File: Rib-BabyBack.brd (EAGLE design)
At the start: 67.3 x 74.9 mm, 27 parts, among them IC1 REG1117, SW1 DPDT

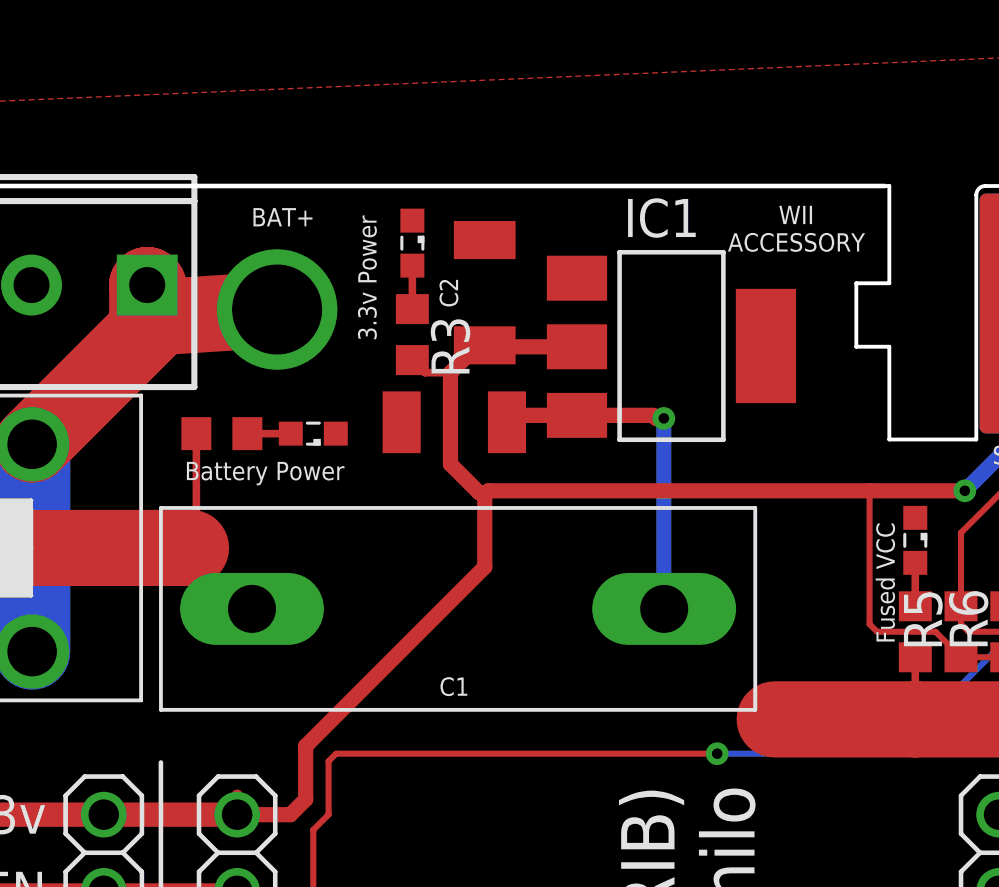
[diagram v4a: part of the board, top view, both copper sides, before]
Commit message: Issue #21 Added a pad for a PTC resetabble fuse for the 3.3v rail
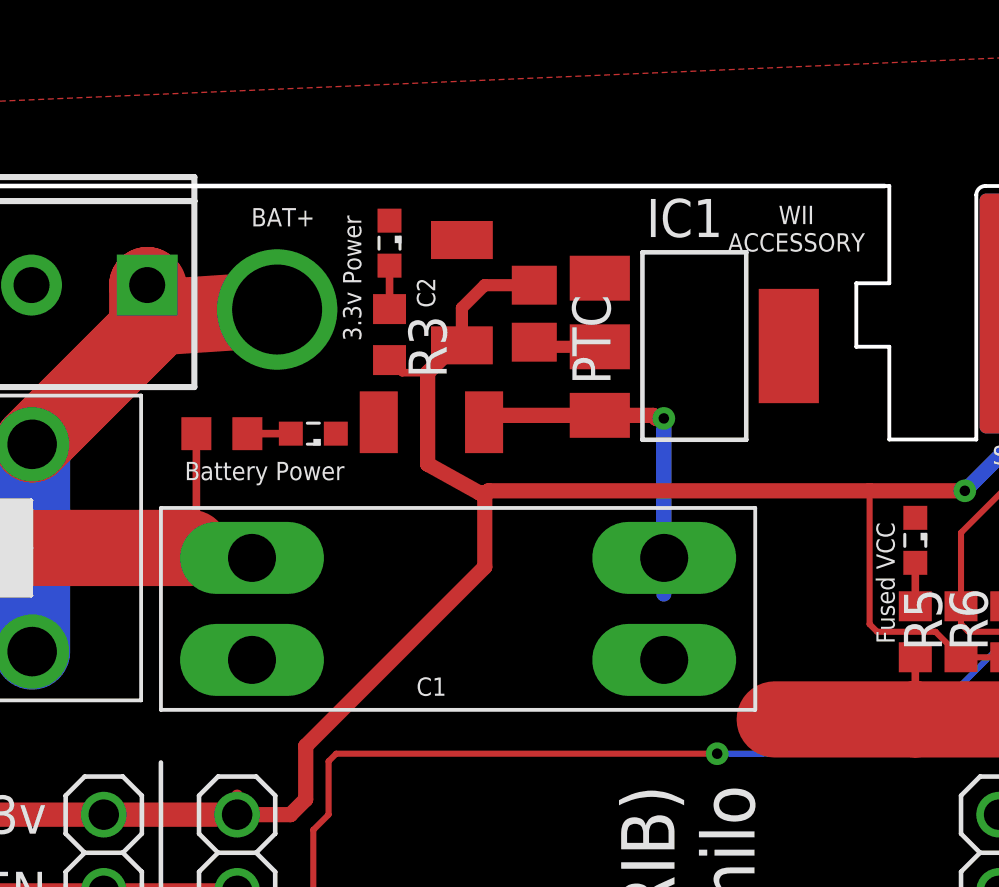
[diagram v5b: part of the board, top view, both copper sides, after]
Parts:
- added PTC: (no value), resistor:R0805
- moved C1 0.76 mm to (27.8, 67.7)
- moved C2 0.76 mm to (28.8, 72.0)
- moved IC1 0.76 mm to (36.6, 70.2)
- moved LED3 0.76 mm to (26.4, 73.7)
- moved R3 0.76 mm to (26.4, 70.6)
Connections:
- new net N$7: IC1.2, PTC.2
- net LIPORAW: now also F4.P$3
- net V3.3: now also PTC.1; no longer IC1.2
- net VCC: now also F4.P$4
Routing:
- net N$7: track 0.00 -> 2.25 mm
- net V3.3: track 119.5 -> 120.7 mm
- net VCC: track 131.2 -> 131.9 mm

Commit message: Issues #33 and 4 and #36
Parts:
- added JP9: (no value), jumper:JP2
- moved LED4 8.44 mm to (11.9, 21.6)
- moved R4 5.39 mm to (13.7, 21.6), turned to 270 degrees
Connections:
- removed net V3.3: C2.1, JP2.19, JP3.19, JP4.1, JP4.10, JP4.11, JP4.12, JP4.13, JP4.14, JP4.15, JP4.16, JP4.17, JP4.18, JP4.19, JP4.2, JP4.3, JP4.4, JP4.5, JP4.6, JP4.7, JP4.8, JP4.9, JP6.19, PTC.1, R3.2, R5.1, R6.1, U$5.PWR
- new net 3V3: JP2.19, JP3.19, JP6.19, JP9.1, R5.1, R6.1, U$5.PWR
- new net SENSORV: JP4.1, JP4.10, JP4.11, JP4.12, JP4.13, JP4.14, JP4.15, JP4.16, JP4.17, JP4.18, JP4.19, JP4.2, JP4.3, JP4.4, JP4.5, JP4.6, JP4.7, JP4.8, JP4.9, JP9.2
- net 5V: now also C2.1, JP9.3, PTC.1, R3.2
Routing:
- net V3.3: track 120.7 -> 0.00 mm, vias 1 -> 0
- net 5V: track 12.7 -> 111.1 mm, vias 0 -> 1
- net 3V3: track 0.00 -> 90.1 mm
- net SENSORV: track 0.00 -> 59.7 mm
- net GND: track 34.2 -> 26.0 mm
- net VCC: track 131.9 -> 139.9 mm
- net LIPORAW: track 29.9 -> 35.5 mm
- net DET: track 73.4 -> 77.1 mm, vias 3 -> 4

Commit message: Issue #34
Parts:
- added D1: (no value), adafruit:SOD-523
- moved PTC 2.29 mm to (31.2, 73.6)
- moved C2 0.36 mm to (28.6, 72.3)
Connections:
- new net N$6: C2.1, D1.A, PTC.1
- net 5V: now also D1.K; no longer C2.1, PTC.1
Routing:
- net N$6: track 0.00 -> 7.26 mm
- net 5V: track 111.1 -> 109.0 mm
- net N$7: track 2.25 -> 3.34 mm
- net GND: vias 5 -> 10
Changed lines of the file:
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@@
 <attribute name="NAME" x="27.813" y="59.182" size="0.6096" layer="25" font="vector" ratio="20" rot="R180" align="bottom-center"/>
 </element>
-<element name="C2" library="SparkFun-Capacitors" package="1210" value="22UF-1210-16V-20%" x="28.829" y="72.009" smashed="yes" rot="R90">
-<attribute name="NAME" x="27.94" y="72.009" size="0.6096" layer="25" font="vector" ratio="20" rot="R90" align="bottom-center"/>
+<element name="C2" library="SparkFun-Capacitors" package="1210" value="22UF-1210-16V-20%" x="28.575" y="72.263" smashed="yes" rot="R90">
+<attribute name="NAME" x="27.686" y="72.263" size="0.6096" layer="25" font="vector" ratio="20" rot="R90" align="bottom-center"/>
 </element>
 <element name="SW1" library="GF-126-0327" package="GF-126-0327" value="DPDT" x="9.906" y="63.5" smashed="yes"/>
@@
 <element name="R5" library="resistor" library_urn="urn:adsk.eagle:library:348" package="R0603" package3d_urn="urn:adsk.eagle:package:26057/1" value="" x="45.466" y="60.706" rot="R90"/>
 <element name="R6" library="resistor" library_urn="urn:adsk.eagle:library:348" package="R0603" package3d_urn="urn:adsk.eagle:package:26057/1" value="" x="46.99" y="60.706" rot="R90"/>
-<element name="PTC" library="resistor" library_urn="urn:adsk.eagle:library:348" package="R0805" package3d_urn="urn:adsk.eagle:package:26059/1" value="" x="31.242" y="71.308" rot="R270"/>
+<element name="PTC" library="resistor" library_urn="urn:adsk.eagle:library:348" package="R0805" package3d_urn="urn:adsk.eagle:package:26059/1" value="" x="31.242" y="73.594" rot="R270"/>
 <element name="JP9" library="jumper" library_urn="urn:adsk.eagle:library:252" package="JP2" package3d_urn="urn:adsk.eagle:package:15452/1" value="" x="12.7" y="13.716" rot="R90"/>
+<element name="D1" library="adafruit" package="SOD-523" value="" x="31.242" y="70.104" rot="R180"/>
 </elements>
 <signals>
@@
 <contactref element="LED4" pad="C"/>
 <contactref element="J1" pad="2"/>
-<wire x1="43.942" y1="64.504" x2="51.562" y2="66.929" width="0" layer="19" extent="1-1"/>
+<via x="27.94" y="72.644" extent="1-16" drill="0.35"/>
+<via x="29.21" y="72.644" extent="1-16" drill="0.35"/>
+<via x="35.306" y="73.66" extent="1-16" drill="0.35"/>
+<via x="35.306" y="72.644" extent="1-16" drill="0.35"/>
+<via x="35.306" y="71.628" extent="1-16" drill="0.35"/>
+<wire x1="51.562" y1="66.929" x2="43.942" y2="64.504" width="0" layer="19" extent="1-1"/>
 </signal>
 <signal name="N$12">
@@
 <wire x1="29.6545" y1="65.3415" x2="29.4005" y2="65.3415" width="0.508" layer="1"/>
 <wire x1="29.4005" y1="65.3415" x2="27.686" y2="66.294" width="0.508" layer="1"/>
-<wire x1="27.686" y1="66.294" x2="27.686" y2="69.342" width="0.508" layer="1"/>
-<wire x1="27.686" y1="69.342" x2="28.598" y2="70.254" width="0.508" layer="1"/>
+<wire x1="27.686" y1="66.294" x2="27.686" y2="68.58" width="0.508" layer="1"/>
 <contactref element="R3" pad="2"/>
 <wire x1="26.416" y1="69.762" x2="26.836" y2="69.342" width="0.254" layer="1"/>
@@
 <wire x1="42.672" y1="60.706" x2="42.418" y2="60.96" width="0.2032" layer="1"/>
 <wire x1="42.418" y1="60.96" x2="42.418" y2="65.405" width="0.2032" layer="1"/>
-<contactref element="PTC" pad="1"/>
-<contactref element="C2" pad="1"/>
-<wire x1="31.242" y1="72.258" x2="29.586" y2="72.258" width="0.4064" layer="1"/>
-<wire x1="28.829" y1="71.501" x2="28.829" y2="70.254" width="0.4064" layer="1"/>
-<wire x1="29.586" y1="72.258" x2="28.829" y2="71.501" width="0.4064" layer="1"/>
 <wire x1="16.891" y1="8.89" x2="14.986" y2="10.795" width="0.6096" layer="1"/>
 <wire x1="14.986" y1="15.494" x2="14.986" y2="10.795" width="0.6096" layer="1"/>
@@
 <wire x1="22.86" y1="10.16" x2="22.86" y2="54.356" width="0.508" layer="1"/>
 <wire x1="22.86" y1="54.356" x2="23.622" y2="55.118" width="0.508" layer="1"/>
-<wire x1="28.598" y1="70.254" x2="28.829" y2="70.254" width="0" layer="19" extent="1-1"/>
+<contactref element="D1" pad="K"/>
+<wire x1="31.242" y1="69.304" x2="28.41" y2="69.304" width="0.254" layer="1"/>
+<wire x1="28.41" y1="69.304" x2="27.686" y2="68.58" width="0.254" layer="1"/>
+<wire x1="28.41" y1="69.304" x2="27.686" y2="69.342" width="0" layer="19" extent="1-1"/>
 <wire x1="8.636" y1="8.89" x2="14.986" y2="10.795" width="0" layer="19" extent="1-1"/>
 </signal>
@@
 <contactref element="PTC" pad="2"/>
 <contactref element="IC1" pad="2"/>
-<wire x1="33.4264" y1="70.2056" x2="31.3944" y2="70.2056" width="0.4064" layer="1"/>
-<wire x1="31.3944" y1="70.2056" x2="31.242" y2="70.358" width="0.4064" layer="1"/>
+<wire x1="33.4264" y1="70.2056" x2="31.242" y2="72.39" width="0.4064" layer="1"/>
+<wire x1="31.242" y1="72.39" x2="31.242" y2="72.644" width="0.4064" layer="1"/>
 </signal>
 <signal name="3V3">
@@
 <wire x1="6.096" y1="54.61" x2="6.096" y2="52.07" width="0" layer="19" extent="1-1"/>
 </signal>
+<signal name="N$6">
+<contactref element="PTC" pad="1"/>
+<contactref element="D1" pad="A"/>
+<contactref element="C2" pad="1"/>
+<wire x1="28.575" y1="70.508" x2="29.479" y2="70.904" width="0.4064" layer="1"/>
+<wire x1="29.479" y1="70.904" x2="30.226" y2="70.904" width="0.4064" layer="1"/>
+<wire x1="30.226" y1="70.904" x2="31.242" y2="70.904" width="0.4064" layer="1"/>
+<wire x1="30.226" y1="70.904" x2="30.1364" y2="70.9936" width="0.4064" layer="1"/>
+<wire x1="30.602" y1="74.544" x2="31.242" y2="74.544" width="0.4064" layer="1"/>
+<wire x1="30.1364" y1="70.9936" x2="30.1364" y2="74.0784" width="0.4064" layer="1"/>
+<wire x1="30.1364" y1="74.0784" x2="30.602" y2="74.544" width="0.4064" layer="1"/>
+</signal>
 </signals>

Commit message: Resolved issue 37
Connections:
- net 5V: now also JP4.14, JP4.15, JP4.16, JP4.17, JP4.18, JP4.19
- net SENSORV: no longer JP4.14, JP4.15, JP4.16, JP4.17, JP4.18, JP4.19
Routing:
- net 5V: track 109.0 -> 141.0 mm, vias 1 -> 3
- net SENSORV: track 59.7 -> 44.5 mm
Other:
- board text added: "34"
- board text added: "35"
- board text added: "36"
- board text added: "39"
- board text added: "5"
- board text removed: "IO34"
- board text removed: "IO35"
- board text removed: "IO36"
- board text removed: "IO39"
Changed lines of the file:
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@@
 <text x="14.986" y="51.435" size="1.27" layer="21" font="vector" ratio="20" align="bottom-right">EN</text>
 <text x="14.986" y="53.975" size="1.27" layer="21" font="vector" ratio="20" align="bottom-right">3.3v</text>
-<text x="14.986" y="48.895" size="1.27" layer="21" font="vector" ratio="20" align="bottom-right">IO36</text>
-<text x="14.986" y="46.355" size="1.27" layer="21" font="vector" ratio="20" align="bottom-right">IO39</text>
-<text x="14.986" y="43.815" size="1.27" layer="21" font="vector" ratio="20" align="bottom-right">IO34</text>
-<text x="14.986" y="41.275" size="1.27" layer="21" font="vector" ratio="20" align="bottom-right">IO35</text>
+<text x="14.986" y="48.895" size="1.27" layer="21" font="vector" ratio="20" align="bottom-right">36</text>
+<text x="14.986" y="46.355" size="1.27" layer="21" font="vector" ratio="20" align="bottom-right">39</text>
+<text x="14.986" y="43.815" size="1.27" layer="21" font="vector" ratio="20" align="bottom-right">34</text>
+<text x="14.986" y="41.275" size="1.27" layer="21" font="vector" ratio="20" align="bottom-right">35</text>
 <text x="14.986" y="38.735" size="1.27" layer="21" font="vector" ratio="20" align="bottom-right">IO32</text>
 <text x="14.986" y="36.195" size="1.27" layer="21" font="vector" ratio="20" align="bottom-right">IO33</text>
@@
 <text x="25.1714" y="72.4916" size="0.6096" layer="21" font="vector" ratio="20" rot="R90" align="center">3.3v Power</text>
 <text x="22.2504" y="66.0654" size="0.6096" layer="21" font="vector" ratio="20" rot="R180" align="center">Battery Power</text>
+<text x="11.43" y="48.895" size="1.27" layer="21" font="vector" ratio="20" align="bottom-right">5</text>
+<text x="11.43" y="46.355" size="1.27" layer="21" font="vector" ratio="20" align="bottom-right">5</text>
+<text x="11.43" y="43.815" size="1.27" layer="21" font="vector" ratio="20" align="bottom-right">5</text>
+<text x="11.43" y="41.275" size="1.27" layer="21" font="vector" ratio="20" align="bottom-right">5</text>
 </plain>
 <attributes>
@@
 <via x="35.306" y="72.644" extent="1-16" drill="0.35"/>
 <via x="35.306" y="71.628" extent="1-16" drill="0.35"/>
-<wire x1="51.562" y1="66.929" x2="43.942" y2="64.504" width="0" layer="19" extent="1-1"/>
+<wire x1="43.942" y1="64.504" x2="51.562" y2="66.929" width="0" layer="19" extent="1-1"/>
 </signal>
 <signal name="N$12">
@@
 <wire x1="31.242" y1="69.304" x2="28.41" y2="69.304" width="0.254" layer="1"/>
 <wire x1="28.41" y1="69.304" x2="27.686" y2="68.58" width="0.254" layer="1"/>
+<contactref element="JP4" pad="15"/>
+<contactref element="JP4" pad="19"/>
+<contactref element="JP4" pad="16"/>
+<contactref element="JP4" pad="17"/>
+<contactref element="JP4" pad="18"/>
+<contactref element="JP4" pad="14"/>
+<wire x1="6.096" y1="41.91" x2="6.096" y2="44.45" width="1.27" layer="1"/>
+<wire x1="6.096" y1="44.45" x2="6.096" y2="46.99" width="1.27" layer="1"/>
+<wire x1="6.096" y1="46.99" x2="6.096" y2="49.53" width="1.27" layer="1"/>
+<wire x1="6.096" y1="49.53" x2="6.096" y2="52.07" width="1.27" layer="1"/>
+<wire x1="6.096" y1="52.07" x2="6.096" y2="54.61" width="1.27" layer="1"/>
+<wire x1="6.096" y1="54.61" x2="6.096" y2="56.134" width="1.27" layer="1"/>
+<via x="6.096" y="56.134" extent="1-16" drill="0.35"/>
+<via x="10.414" y="56.134" extent="1-16" drill="0.35"/>
+<wire x1="6.096" y1="56.134" x2="7.9688125" y2="56.134" width="1.27" layer="16"/>
+<wire x1="7.9688125" y1="56.134" x2="7.9942125" y2="56.1594" width="1.27" layer="16"/>
+<wire x1="7.9942125" y1="56.1594" x2="9.2777875" y2="56.1594" width="1.27" layer="16"/>
+<wire x1="9.2777875" y1="56.1594" x2="9.3031875" y2="56.134" width="1.27" layer="16"/>
+<wire x1="9.3031875" y1="56.134" x2="10.414" y2="56.134" width="1.27" layer="16"/>
+<wire x1="10.414" y1="56.134" x2="22.86" y2="56.134" width="0.4064" layer="1"/>
+<wire x1="22.86" y1="56.134" x2="23.622" y2="56.896" width="0.4064" layer="1"/>
 <wire x1="28.41" y1="69.304" x2="27.686" y2="69.342" width="0" layer="19" extent="1-1"/>
 <wire x1="8.636" y1="8.89" x2="14.986" y2="10.795" width="0" layer="19" extent="1-1"/>
@@
 <contactref element="JP4" pad="10"/>
 <contactref element="JP4" pad="11"/>
-<contactref element="JP4" pad="19"/>
 <contactref element="JP4" pad="12"/>
 <contactref element="JP4" pad="13"/>
-<contactref element="JP4" pad="14"/>
-<contactref element="JP4" pad="15"/>
-<contactref element="JP4" pad="16"/>
-<contactref element="JP4" pad="17"/>
-<contactref element="JP4" pad="18"/>
-<wire x1="6.096" y1="54.61" x2="6.096" y2="8.89" width="1.27" layer="1"/>
 <wire x1="6.096" y1="8.89" x2="6.096" y2="7.62" width="0.6096" layer="1"/>
 <wire x1="6.096" y1="7.62" x2="6.858" y2="6.858" width="0.6096" layer="1"/>
@@
 <wire x1="10.668" y1="12.954" x2="11.43" y2="13.716" width="0.6096" layer="1"/>
 <wire x1="11.43" y1="13.716" x2="12.7" y2="13.716" width="0.6096" layer="1"/>
-<wire x1="6.096" y1="49.53" x2="6.096" y2="52.07" width="0" layer="19" extent="1-1"/>
-<wire x1="6.096" y1="46.99" x2="6.096" y2="49.53" width="0" layer="19" extent="1-1"/>
-<wire x1="6.096" y1="44.45" x2="6.096" y2="46.99" width="0" layer="19" extent="1-1"/>
-<wire x1="6.096" y1="41.91" x2="6.096" y2="44.45" width="0" layer="19" extent="1-1"/>
-<wire x1="6.096" y1="39.37" x2="6.096" y2="41.91" width="0" layer="19" extent="1-1"/>
-<wire x1="6.096" y1="36.83" x2="6.096" y2="39.37" width="0" layer="19" extent="1-1"/>
-<wire x1="6.096" y1="34.29" x2="6.096" y2="36.83" width="0" layer="19" extent="1-1"/>
-<wire x1="6.096" y1="31.75" x2="6.096" y2="34.29" width="0" layer="19" extent="1-1"/>
-<wire x1="6.096" y1="29.21" x2="6.096" y2="31.75" width="0" layer="19" extent="1-1"/>
-<wire x1="6.096" y1="26.67" x2="6.096" y2="29.21" width="0" layer="19" extent="1-1"/>
-<wire x1="6.096" y1="24.13" x2="6.096" y2="26.67" width="0" layer="19" extent="1-1"/>
-<wire x1="6.096" y1="21.59" x2="6.096" y2="24.13" width="0" layer="19" extent="1-1"/>
-<wire x1="6.096" y1="19.05" x2="6.096" y2="21.59" width="0" layer="19" extent="1-1"/>
-<wire x1="6.096" y1="16.51" x2="6.096" y2="19.05" width="0" layer="19" extent="1-1"/>
-<wire x1="6.096" y1="13.97" x2="6.096" y2="16.51" width="0" layer="19" extent="1-1"/>
-<wire x1="6.096" y1="11.43" x2="6.096" y2="13.97" width="0" layer="19" extent="1-1"/>
-<wire x1="6.096" y1="54.61" x2="6.096" y2="52.07" width="0" layer="19" extent="1-1"/>
+<wire x1="6.096" y1="8.89" x2="6.096" y2="11.43" width="1.27" layer="1"/>
+<wire x1="6.096" y1="11.43" x2="6.096" y2="13.97" width="1.27" layer="1"/>
+<wire x1="6.096" y1="13.97" x2="6.096" y2="16.51" width="1.27" layer="1"/>
+<wire x1="6.096" y1="16.51" x2="6.096" y2="19.05" width="1.27" layer="1"/>
+<wire x1="6.096" y1="19.05" x2="6.096" y2="21.59" width="1.27" layer="1"/>
+<wire x1="6.096" y1="21.59" x2="6.096" y2="24.13" width="1.27" layer="1"/>
+<wire x1="6.096" y1="24.13" x2="6.096" y2="26.67" width="1.27" layer="1"/>
+<wire x1="6.096" y1="26.67" x2="6.096" y2="29.21" width="1.27" layer="1"/>
+<wire x1="6.096" y1="29.21" x2="6.096" y2="31.75" width="1.27" layer="1"/>
+<wire x1="6.096" y1="31.75" x2="6.096" y2="34.29" width="1.27" layer="1"/>
+<wire x1="6.096" y1="34.29" x2="6.096" y2="36.83" width="1.27" layer="1"/>
+<wire x1="6.096" y1="36.83" x2="6.096" y2="39.37" width="1.27" layer="1"/>
 </signal>
 <signal name="N$6">
